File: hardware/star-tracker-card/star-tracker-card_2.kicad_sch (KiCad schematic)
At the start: 88 parts, among them Q2 DMN3028LQ-7, Q3 DMP2240UDM, Q4 DMN3028LQ-7, Q5 DMP3050LVT-7, Q6 DMP3050LVT-7, U12 MIC842LYC5, U13 MIC842LYC5, U14 MAX4211FETE, U15 TPS62112, U16 MAX7310ATE, U2 TS5A21366DCUR

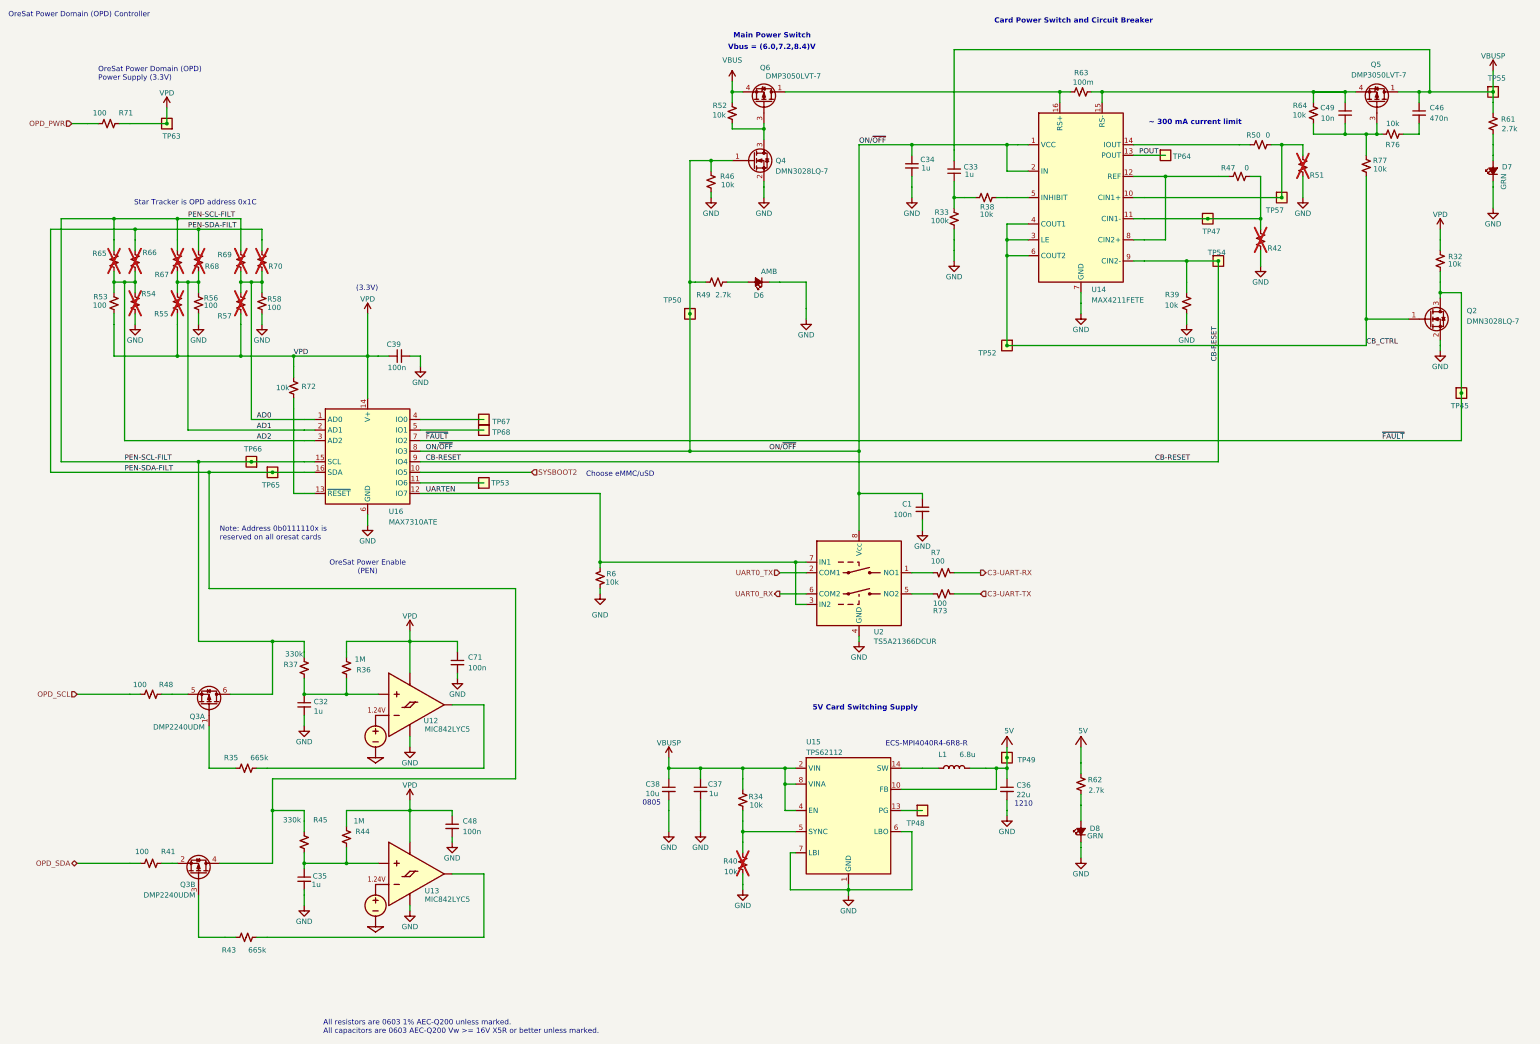
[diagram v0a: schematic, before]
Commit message: Updates to BOM to get v1.3r1
All transistors upgraded, OPD circuit breaker cutoff raised to 924 mA.
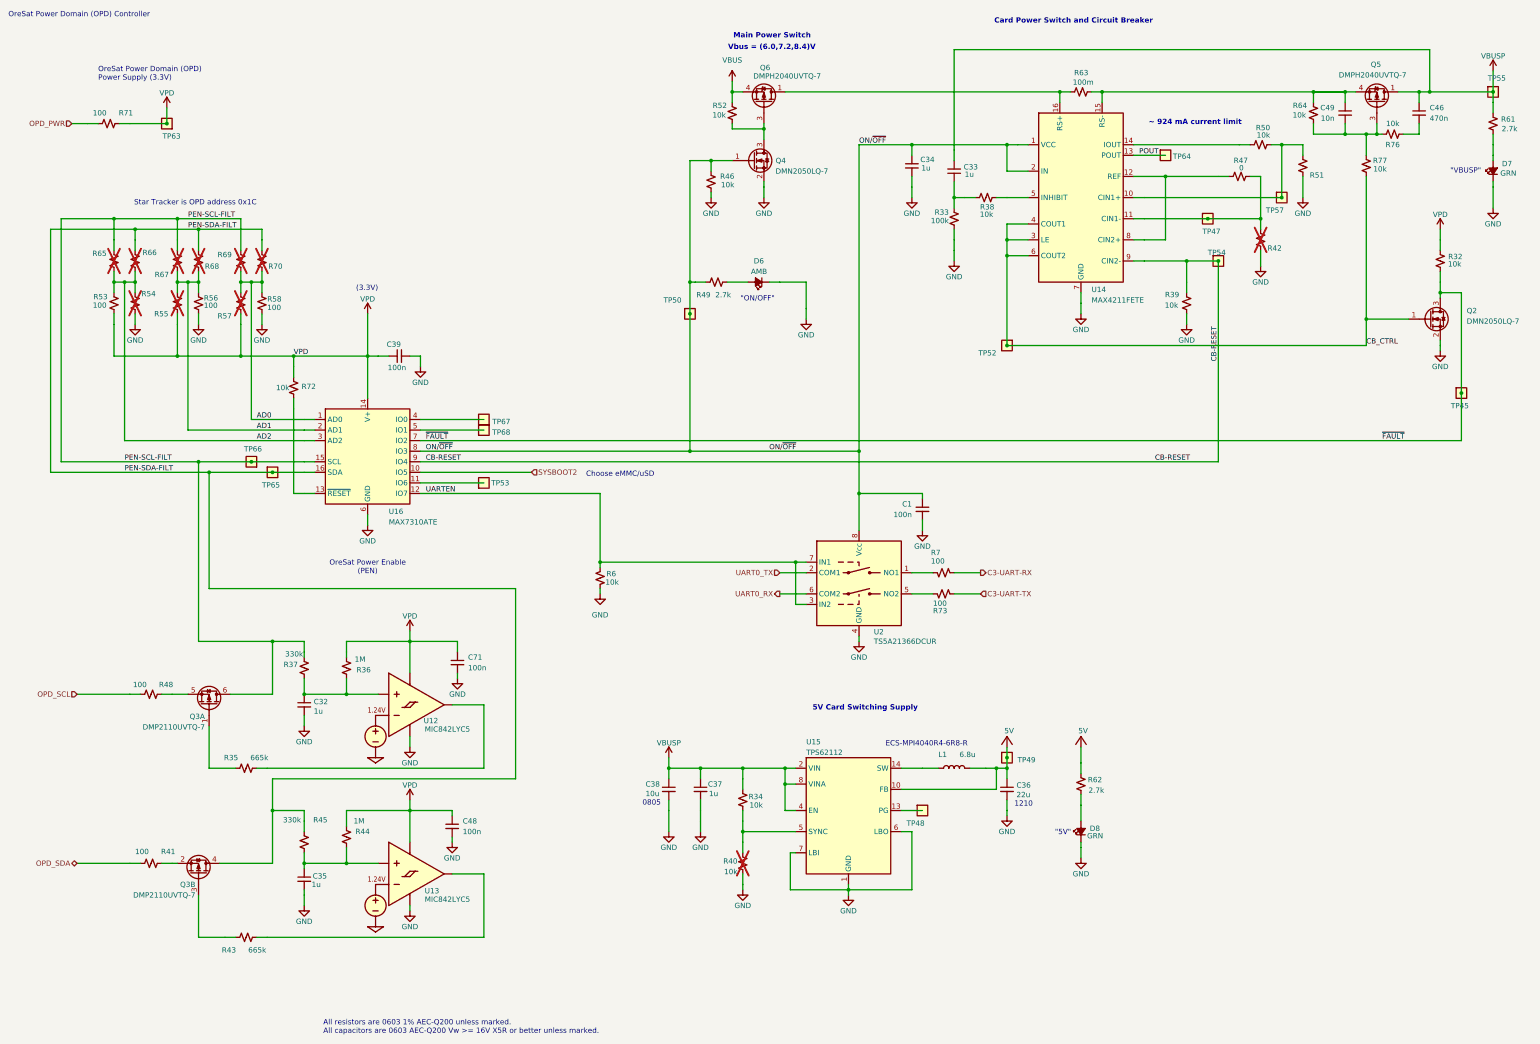
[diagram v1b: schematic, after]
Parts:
- Q2, Q4: value DMN3028LQ-7 -> DMN2050LQ-7; DPN 31-DMN3028LQ-7CT-ND -> 31-DMN2050LQ-7CT-ND; MPN DMN3028LQ-7 -> DMN2050LQ-7
- Q3: value DMP2240UDM -> DMP2110UVTQ-7; DPN DMP2240UDMDICT-ND -> 31-DMP2110UVTQ-7CT-ND; MFR Diodes Inc -> Diodes Incorporated; MPN DMP2240UDM-7 -> DMP2110UVTQ-7
- Q5, Q6: value DMP3050LVT-7 -> DMPH2040UVTQ-7; DPN 31-DMP3050LVTQ-7-ND -> 31-DMPH2040UVTQ-7CT-ND; MFR Diodes Inc -> Diodes Incorporated; MPN DMP3050LVTQ-7 -> DMPH2040UVTQ-7
- R50: value 0 -> 10k; DPN RMCF0603ZT0R00CT-ND -> RMCF0603FT10K0CT-ND; MPN RMCF0603ZT0R00 -> RMCF0603FT10K0
- R51: value NP -> 4.7k; DIS Digi-Key -> DigiKey; DPN 1276-4275-1-ND -> RMCF0603FT4K70CT-ND; MFR Samsung -> Stackpole Electronics; MPN RC1005F6653CS -> RMCF0603FT4K70; now fitted
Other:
- note added: ""5V""
- note added: ""ON/OFF""
- note added: ""VBUSP""
- note added: "~ 924 mA current limit"
- note removed: "Note: Address 0b0111110x is reserved on all oresat cards"
- note removed: "~ 300 mA current limit"
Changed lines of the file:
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@@
 		)
 	)
+	(text "\"VBUSP\""
+		(exclude_from_sim no)
+		(at 387.096 58.42 0)
+		(effects
+			(font
+				(size 1.27 1.27)
+			)
+		)
+	)
 	(text "ECS-MPI4040R4-6R8-R"
 		(exclude_from_sim no)
@@
 		)
 	)
+	(text "\"ON/OFF\""
+		(exclude_from_sim no)
+		(at 216.916 89.154 0)
+		(effects
+			(font
+				(size 1.27 1.27)
+			)
+		)
+	)
 	(text "OreSat Power Domain (OPD) Controller"
 		(exclude_from_sim no)
@@
 		)
 	)
-	(text "~ 300 mA current limit"
+	(text "\"5V\""
 		(exclude_from_sim no)
-		(at 310.896 47.498 0)
+		(at 290.322 217.424 0)
 		(effects
 			(font
 				(size 1.27 1.27)
-				(thickness 0.254)
-				(bold yes)
 			)
-			(justify left bottom)
 		)
 	)
-	(text "Note: Address 0b0111110x is\nreserved on all oresat cards"
+	(text "~ 924 mA current limit"
 		(exclude_from_sim no)
-		(at 87.63 147.32 0)
+		(at 310.896 47.498 0)
 		(effects
 			(font
 				(size 1.27 1.27)
+				(thickness 0.254)
+				(bold yes)
 			)
 			(justify left bottom)
@@
 			)
 		)
-		(property "Value" "DMP2240UDM"
+		(property "Value" "DMP2110UVTQ-7"
 			(at 81.788 233.172 90)
 			(show_name no)
@@
 			)
 		)
-		(property "Datasheet" "https://www.diodes.com/assets/Datasheets/ds31197.pdf"
+		(property "Datasheet" "https://www.diodes.com/assets/Datasheets/DMP2110UVTQ.pdf"
 			(at 82.55 226.06 0)
 			(hide yes)
@@
 			)
 		)
-		(property "Description" "Mosfet Array 2 P-Channel (Dual) 20V 2A 600mW Surface Mount SOT-26"
+		(property "Description" "Mosfet Array 20V 1.8A (Ta) 740mW (Ta) Surface Mount TSOT-26"
 			(at 82.55 227.33 0)
 			(hide yes)
@@
 			)
 		)
-		(property "DPN" "DMP2240UDMDICT-ND"
+		(property "DPN" "31-DMP2110UVTQ-7CT-ND"
 			(at 82.55 227.33 90)
 			(hide yes)
@@
 			)
 		)
-		(property "MFR" "Diodes Inc"
+		(property "MFR" "Diodes Incorporated"
 			(at 82.55 227.33 90)
 			(hide yes)
@@
 			)
 		)
-		(property "MPN" "DMP2240UDM-7"
+		(property "MPN" "DMP2110UVTQ-7"
 			(at 82.55 227.33 90)
 			(hide yes)
@@
 		(dnp no)
 		(property "Reference" "D6"
-			(at 218.44 88.265 0)
+			(at 218.44 80.01 0)
 			(show_name no)
 			(do_not_autoplace no)
@@
 		)
 		(property "Value" "AMB"
-			(at 221.615 82.55 0)
+			(at 219.202 82.55 0)
 			(show_name no)
 			(do_not_autoplace no)
@@
 			)
 		)
-		(property "Value" "DMP3050LVT-7"
+		(property "Value" "DMPH2040UVTQ-7"
 			(at 232.156 36.322 90)
 			(show_name no)
@@
 			)
 		)
-		(property "Datasheet" "https://www.diodes.com/assets/Datasheets/DMP3050LVTQ.pdf"
+		(property "Datasheet" "https://www.diodes.com/assets/Datasheets/DMPH2040UVTQ.pdf"
 			(at 218.44 41.91 90)
 			(hide yes)
@@
 			)
 		)
-		(property "Description" "P-Channel 30 V 4.5A (Ta) 1.6W (Ta) Surface Mount TSOT-26"
+		(property "Description" "P-Channel 20 V 5.6A (Ta), 11.7A (Tc) 1W (Ta) Surface Mount TSOT-26"
 			(at 218.44 41.91 0)
 			(hide yes)
@@
 			)
 		)
-		(property "MPN" "DMP3050LVTQ-7"
+		(property "MPN" "DMPH2040UVTQ-7"
 			(at 218.44 41.91 0)
 			(hide yes)
@@
 			)
 		)
-		(property "DPN" "31-DMP3050LVTQ-7-ND"
+		(property "DPN" "31-DMPH2040UVTQ-7CT-ND"
 			(at 218.44 41.91 90)
 			(hide yes)
@@
 			)
 		)
-		(property "MFR" "Diodes Inc"
+		(property "MFR" "Diodes Incorporated"
 			(at 218.44 41.91 90)
 			(hide yes)
@@
 			)
 		)
-		(property "Value" "DMN3028LQ-7"
+		(property "Value" "DMN2050LQ-7"
 			(at 387.35 95.25 0)
 			(show_name no)
@@
 			)
 		)
-		(property "Datasheet" "https://www.diodes.com/assets/Datasheets/DMN3028LQ.pdf"
+		(property "Datasheet" "https://www.diodes.com/datasheet/download/DMN2050LQ.pdf"
 			(at 378.46 93.98 0)
 			(hide yes)
@@
 			)
 		)
-		(property "Description" "N-Channel 30 V 6.2A (Ta) 860mW (Ta) Surface Mount SOT-23-3 (TO-236)"
+		(property "Description" "N-Channel 20 V 5.9A (Ta) 1.4W Surface Mount SOT-23-3"
 			(at 378.46 93.98 0)
 			(hide yes)
@@
 			)
 		)
-		(property "DPN" "31-DMN3028LQ-7CT-ND"
+		(property "DPN" "31-DMN2050LQ-7CT-ND"
 			(at 378.46 93.98 0)
 			(hide yes)
@@
 			)
 		)
-		(property "MPN" "DMN3028LQ-7"
+		(property "MPN" "DMN2050LQ-7"
 			(at 378.46 93.98 0)
 			(hide yes)
@@
 			)
 		)
-		(property "Value" "DMP3050LVT-7"
+		(property "Value" "DMPH2040UVTQ-7"
 			(at 372.872 36.068 90)
 			(show_name no)
@@
 			)
 		)
-		(property "Datasheet" "https://www.diodes.com/assets/Datasheets/DMP3050LVTQ.pdf"
+		(property "Datasheet" "https://www.diodes.com/assets/Datasheets/DMPH2040UVTQ.pdf"
 			(at 365.76 41.91 90)
 			(hide yes)
@@
 			)
 		)
-		(property "Description" "P-Channel 30 V 4.5A (Ta) 1.6W (Ta) Surface Mount TSOT-26"
+		(property "Description" "P-Channel 20 V 5.6A (Ta), 11.7A (Tc) 1W (Ta) Surface Mount TSOT-26"
 			(at 365.76 41.91 0)
 			(hide yes)
@@
 			)
 		)
-		(property "MPN" "DMP3050LVTQ-7"
+		(property "MPN" "DMPH2040UVTQ-7"
 			(at 365.76 41.91 0)
 			(hide yes)
@@
 			)
 		)
-		(property "DPN" "31-DMP3050LVTQ-7-ND"
+		(property "DPN" "31-DMPH2040UVTQ-7CT-ND"
 			(at 365.76 41.91 90)
 			(hide yes)
@@
 			)
 		)
-		(property "MFR" "Diodes Inc"
+		(property "MFR" "Diodes Incorporated"
 			(at 365.76 41.91 90)
 			(hide yes)
@@
 		(on_board yes)
 		(in_pos_files yes)
-		(dnp yes)
+		(dnp no)
 		(property "Reference" "R51"
 			(at 353.06 58.6486 0)
@@
 			)
 		)
-		(property "Value" "NP"
+		(property "Value" "4.7k"
 			(at 346.71 58.42 0)
 			(hide yes)
@@
 			)
 		)
-		(property "Datasheet" ""
+		(property "Datasheet" "https://www.seielect.com/catalog/SEI-RMCF_RMCP.pdf"
 			(at 347.98 57.15 0)
 			(hide yes)
@@
 			)
 		)
-		(property "Description" "Resistor, small US symbol"
+		(property "Description" "4.7 kOhms ±1% 0.1W, 1/10W Chip Resistor 0603 (1608 Metric) Automotive AEC-Q200 Thick Film"
 			(at 347.98 57.15 0)
 			(hide yes)
@@
 			)
 		)
-		(property "DIS" "Digi-Key"
+		(property "DIS" "DigiKey"
 			(at 347.98 57.15 0)
 			(hide yes)
@@
 			)
 		)
-		(property "DPN" "1276-4275-1-ND"
+		(property "DPN" "RMCF0603FT4K70CT-ND"
 			(at 347.98 57.15 0)
 			(hide yes)
@@
 			)
 		)
-		(property "MFR" "Samsung"
+		(property "MFR" "Stackpole Electronics"
 			(at 347.98 57.15 0)
 			(hide yes)
@@
 			)
 		)
-		(property "MPN" "RC1005F6653CS"
+		(property "MPN" "RMCF0603FT4K70"
 			(at 347.98 57.15 0)
 			(hide yes)
@@
 		(dnp no)
 		(property "Reference" "R50"
-			(at 337.82 49.022 90)
+			(at 340.106 47.244 90)
 			(show_name no)
 			(do_not_autoplace no)
@@
 			)
 		)
-		(property "Value" "0"
+		(property "Value" "10k"
 			(at 340.106 49.022 90)
 			(show_name no)
@@
 			)
 		)
-		(property "Description" "0 Ohms Jumper Chip Resistor 0603 (1608 Metric) Automotive AEC-Q200 Thick Film"
+		(property "Description" "10 kOhms ±1% 0.1W, 1/10W Chip Resistor 0603 (1608 Metric) Automotive AEC-Q200 Thick Film"
 			(at 337.82 52.07 0)
 			(hide yes)
@@
 			)
 		)
-		(property "DPN" "RMCF0603ZT0R00CT-ND"
+		(property "DPN" "RMCF0603FT10K0CT-ND"
 			(at 337.82 52.07 90)
 			(hide yes)
@@
 			)
 		)
-		(property "MPN" "RMCF0603ZT0R00"
+		(property "MPN" "RMCF0603FT10K0"
 			(at 337.82 52.07 90)
 			(hide yes)
@@
 		(dnp no)
 		(property "Reference" "D7"
-			(at 398.272 57.404 90)
+			(at 398.272 56.642 90)
 			(show_name no)
 			(do_not_autoplace no)
@@
 		)
 		(property "Value" "GRN"
-			(at 396.24 62.865 0)
+			(at 399.288 58.928 90)
 			(show_name no)
 			(do_not_autoplace no)
@@
 			)
 		)
-		(property "Value" "DMN3028LQ-7"
+		(property "Value" "DMN2050LQ-7"
 			(at 221.234 59.182 0)
 			(show_name no)
@@
 			)
 		)
-		(property "Datasheet" "https://www.diodes.com/assets/Datasheets/DMN3028LQ.pdf"
+		(property "Datasheet" "https://www.diodes.com/datasheet/download/DMN2050LQ.pdf"
 			(at 215.9 55.88 0)
 			(hide yes)
@@
 			)
 		)
-		(property "Description" "N-Channel 30 V 6.2A (Ta) 860mW (Ta) Surface Mount SOT-23-3 (TO-236)"
+		(property "Description" "N-Channel 20 V 5.9A (Ta) 1.4W Surface Mount SOT-23-3"
 			(at 215.9 55.88 0)
 			(hide yes)
@@
 			)
 		)
-		(property "DPN" "31-DMN3028LQ-7CT-ND"
+		(property "DPN" "31-DMN2050LQ-7CT-ND"
 			(at 215.9 55.88 0)
 			(hide yes)
@@
 			)
 		)
-		(property "MPN" "DMN3028LQ-7"
+		(property "MPN" "DMN2050LQ-7"
 			(at 215.9 55.88 0)
 			(hide yes)
@@
 			)
 		)
-		(property "Value" "DMP2240UDM"
+		(property "Value" "DMP2110UVTQ-7"
 			(at 84.074 192.786 90)
 			(show_name no)
@@
 			)
 		)
-		(property "Datasheet" "https://www.diodes.com/assets/Datasheets/ds31197.pdf"
+		(property "Datasheet" "https://www.diodes.com/assets/Datasheets/DMP2110UVTQ.pdf"
 			(at 85.09 185.42 0)
 			(hide yes)
@@
 			)
 		)
-		(property "Description" "Mosfet Array 2 P-Channel (Dual) 20V 2A 600mW Surface Mount SOT-26"
+		(property "Description" "Mosfet Array 20V 1.8A (Ta) 740mW (Ta) Surface Mount TSOT-26"
 			(at 85.09 186.69 0)
 			(hide yes)
@@
 			)
 		)
-		(property "DPN" "DMP2240UDMDICT-ND"
+		(property "DPN" "31-DMP2110UVTQ-7CT-ND"
 			(at 85.09 186.69 90)
 			(hide yes)
@@
 			)
 		)
-		(property "MFR" "Diodes Inc"
+		(property "MFR" "Diodes Incorporated"
 			(at 85.09 186.69 90)
 			(hide yes)
@@
 			)
 		)
-		(property "MPN" "DMP2240UDM-7"
+		(property "MPN" "DMP2110UVTQ-7"
 			(at 85.09 186.69 90)
 			(hide yes)
@@
 		(dnp no)
 		(property "Reference" "R47"
-			(at 331.724 56.896 90)
+			(at 334.772 55.118 90)
 			(show_name no)
 			(do_not_autoplace no)
@@
 		)
 		(property "Value" "0"
-			(at 335.026 56.896 90)
+			(at 333.756 56.896 90)
 			(show_name no)
 			(do_not_autoplace no)
